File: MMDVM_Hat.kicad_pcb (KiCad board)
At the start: 2 copper layers, 65 x 56 mm, 107 parts, among them J1 Radio, J2 Raspberry_Pi_2_3, J7 GS2, J8 GS3, Q1 IRLML2060, Q2 2N7002, U1 LD1117S33TR, U2 STM32F722RETx, U3 MCP6002, U4 MCP6002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

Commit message: Revision 0.1
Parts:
- removed LEDs: FP_LEDs, Pin_Headers:Pin_Header_Straight_2x05_Pitch2.54mm
- added D10: POCSAG, LEDs:LED_0603, F.Cu at (29.2, 107.6)
- added G***: LOGO, MMDVM_logo:MMDVM_logo, F.Cu at (50.2, 77.7)
- added G***: LOGO, w_logo:Logo_silk_CC-BY-NC-SA_10x3.6mm, B.Cu at (25.2, 115.9)
- added J4: Panel LEDs, Pin_Headers:Pin_Header_Straight_2x10_Pitch2.00mm, F.Cu at (23.2, 107.6)
- added R33: 1k5, Resistors_SMD:R_0603, F.Cu at (32.8, 107.6)
- J7: footprint Connectors:GS2 -> jumper:SolderJumper-2_P1.3mm_Open_TrianglePad1.0x1.5mm
- J8: footprint Connectors:GS3 -> jumper:SolderJumper-3_P2.0mm_Open_TrianglePad1.0x1.5mm
- moved R6 8.31 mm to (32.8, 105.6)
- moved D5 8.30 mm to (29.2, 105.6)
- moved Radio TX 7.75 mm to (26.7, 116.3), turned to 90 degrees
- moved R11 6.11 mm to (32.8, 97.6)
- moved D9 6.10 mm to (29.2, 97.6)
- moved R7 4.71 mm to (32.8, 103.6)
- moved D6 4.70 mm to (29.2, 103.6)
- moved TX 4.35 mm to (31.1, 117.8), turned to 180 degrees
- moved STlink 3.72 mm to (21.5, 112.4)
- moved C22 3.23 mm to (39.0, 100.3)
- moved C23 3.23 mm to (39.0, 98.8)
- moved C11 3.16 mm to (37.5, 108.2), turned to 270 degrees
- moved C12 3.05 mm to (35.8, 108.2), turned to 270 degrees
- moved R9 2.52 mm to (32.8, 99.6)
- moved D8 2.50 mm to (29.2, 99.6)
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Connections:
- U2 pad 26: NXDN_LED -> Net-(U2-Pad26)
- U2 pad 33: Net-(U2-Pad33) -> SVC_LED
- U2 pad 34: PTT -> COS_LED
- U2 pad 35: COS_LED -> PTT
- U2 pad 36: SVC_LED -> DSTAR_LED
- U2 pad 37: Net-(U2-Pad37) -> DMR_LED
- U2 pad 38: DSTAR_LED -> YSF_LED
- U2 pad 39: DMR_LED -> P25_LED
- U2 pad 40: P25_LED -> NXDN_LED
- U2 pad 41: YSF_LED -> POCSAG_LED
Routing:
- net SVC_LED: track 48.3 -> 9.33 mm, vias 1 -> 0
- net COS_LED: track 40.0 -> 9.93 mm, vias 3 -> 0
- net DSTAR_LED: track 31.5 -> 12.0 mm, vias 2 -> 0
- net POCSAG_LED: track 0.00 -> 19.1 mm
- net YSF_LED: track 33.5 -> 14.9 mm, vias 2 -> 0
- net NXDN_LED: track 35.8 -> 17.7 mm, vias 3 -> 0
- net DMR_LED: track 31.0 -> 13.4 mm, vias 2 -> 0
- net +3V3: track 189.3 -> 206.1 mm
- net P25_LED: track 30.2 -> 16.3 mm
- net DAC_TX: track 32.4 -> 44.5 mm, vias 1 -> 2
- net Net-(D10-Pad2): track 0.00 -> 9.95 mm, vias 0 -> 1
- net Net-(D9-Pad2): track 1.75 -> 9.95 mm, vias 0 -> 1
- net Net-(D8-Pad2): track 1.75 -> 9.95 mm, vias 0 -> 1
- net Net-(D7-Pad2): track 1.75 -> 9.95 mm, vias 0 -> 1
- net Net-(D6-Pad2): track 1.75 -> 9.95 mm, vias 0 -> 1
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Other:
- outline, holes or cut-outs redrawn
- board text added: "12.000 MHz"
- board text added: "12.288 MHz"
- board text added: "14.400 MHz"
- board text added: "19.200 MHz"
- board text added: "Direct"
- board text added: "POCSAG"
- board text added: "Panel LEDs"
- board text added: "Revision 0.1"
- board text added: "Serial No:"
- board text added: "TCXO Frequency"
- board text added: "Trimmed"
- board text removed: "D*"

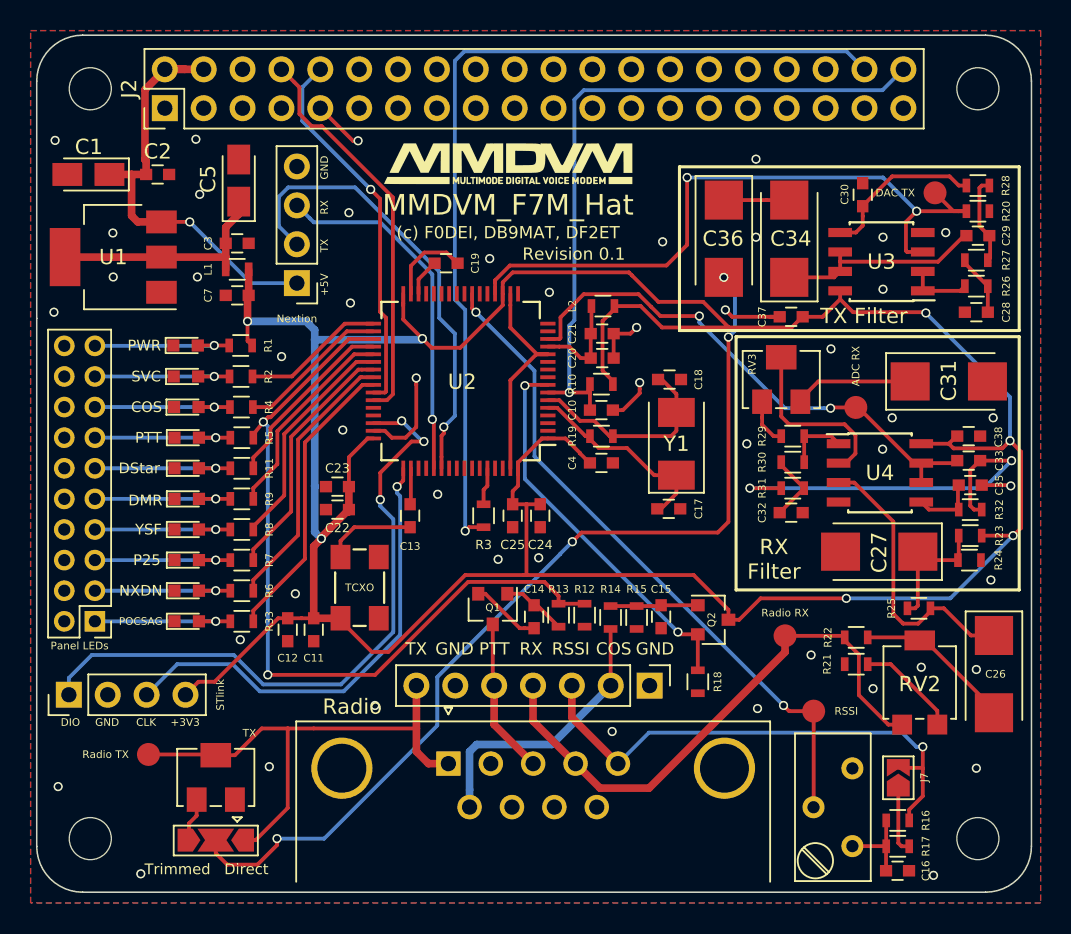
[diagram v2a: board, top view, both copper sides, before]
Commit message: Revision 0.2: Added FET for channel switching; Rename to MMDVM_RPT_Hat
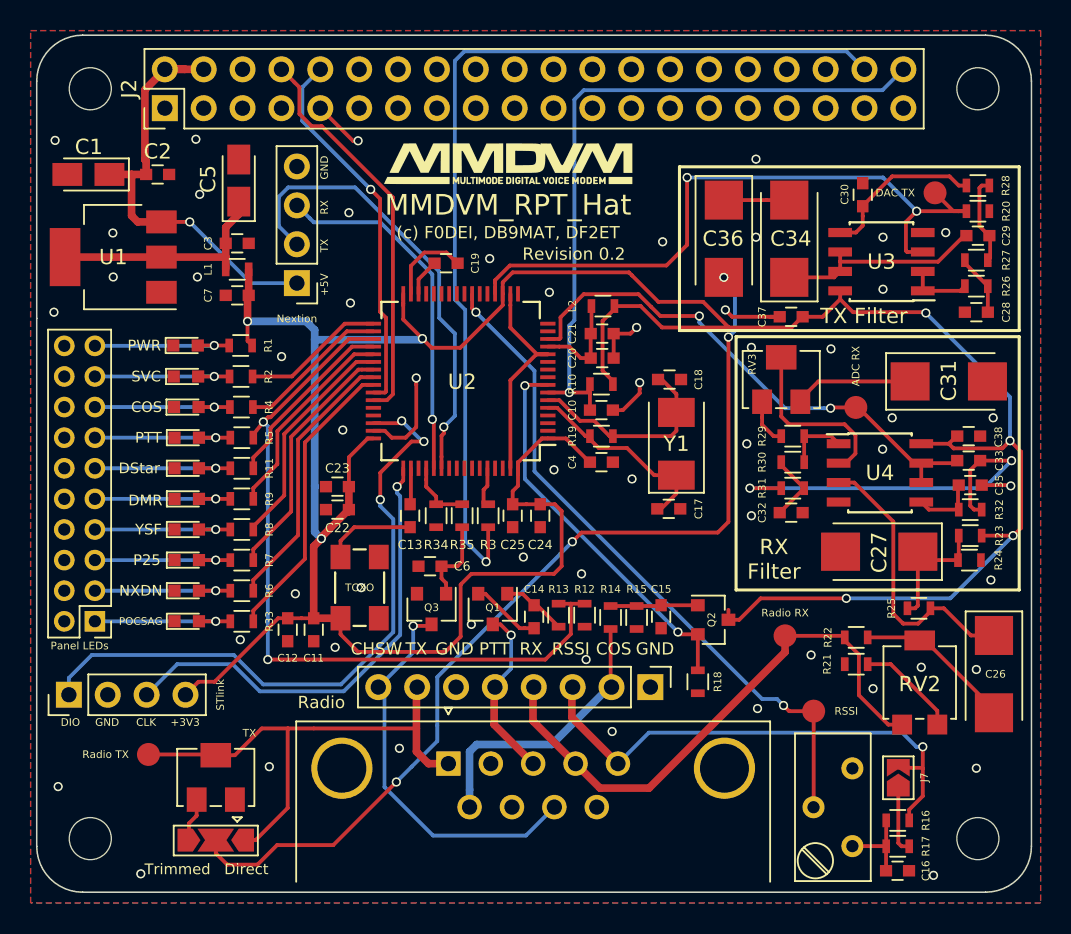
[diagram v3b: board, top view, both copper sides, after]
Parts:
- removed Radio: Radio, Pin_Headers:Pin_Header_Straight_1x07_Pitch2.54mm
- added C6: 470p, Capacitors_SMD:C_0603, F.Cu at (45.1, 104.0)
- added J5: Radio, Pin_Headers:Pin_Header_Straight_1x08_Pitch2.54mm, F.Cu at (59.5, 111.9)
- added Q3: IRLML2060, TO_SOT_Packages_SMD:SOT-23, F.Cu at (45.2, 106.8)
- added R34: 47k, Resistors_SMD:R_0603, F.Cu at (45.5, 100.7)
- added R35: 330, Resistors_SMD:R_0603, F.Cu at (47.2, 100.7)
- R19: value R -> 1M
- moved R3 0.30 mm to (48.9, 100.7)
- turned C4 to 180 degrees
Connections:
- C4 pad 1: +3V3 -> GND
- C4 pad 2: GND -> +3V3
- J1 pad 8: Net-(J1-Pad8) -> RADIO_CH_SW
- U2 pad 52: Net-(U2-Pad52) -> CH_SW
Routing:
- net RADIO_CH_SW: track 0.00 -> 26.1 mm, vias 0 -> 1
- net +3V3: track 206.1 -> 197.7 mm
- net Net-(C6-Pad1): track 0.00 -> 5.65 mm
- net CH_SW: track 0.00 -> 4.32 mm
- net Net-(J2-Pad38): track 59.8 -> 63.4 mm
- net RADIO_PTT: track 10.2 -> 11.5 mm, vias 0 -> 1
- net PTT: track 51.4 -> 50.5 mm
- net RSSI: track 43.7 -> 44.3 mm
- net GND: vias 48 -> 55
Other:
- board text added: "CHSW"
- board text added: "MMDVM_RPT_Hat"
- board text added: "Radio"
- board text added: "Revision 0.2"
- board text removed: "MMDVM_F7M_Hat"
- board text removed: "Revision 0.1"

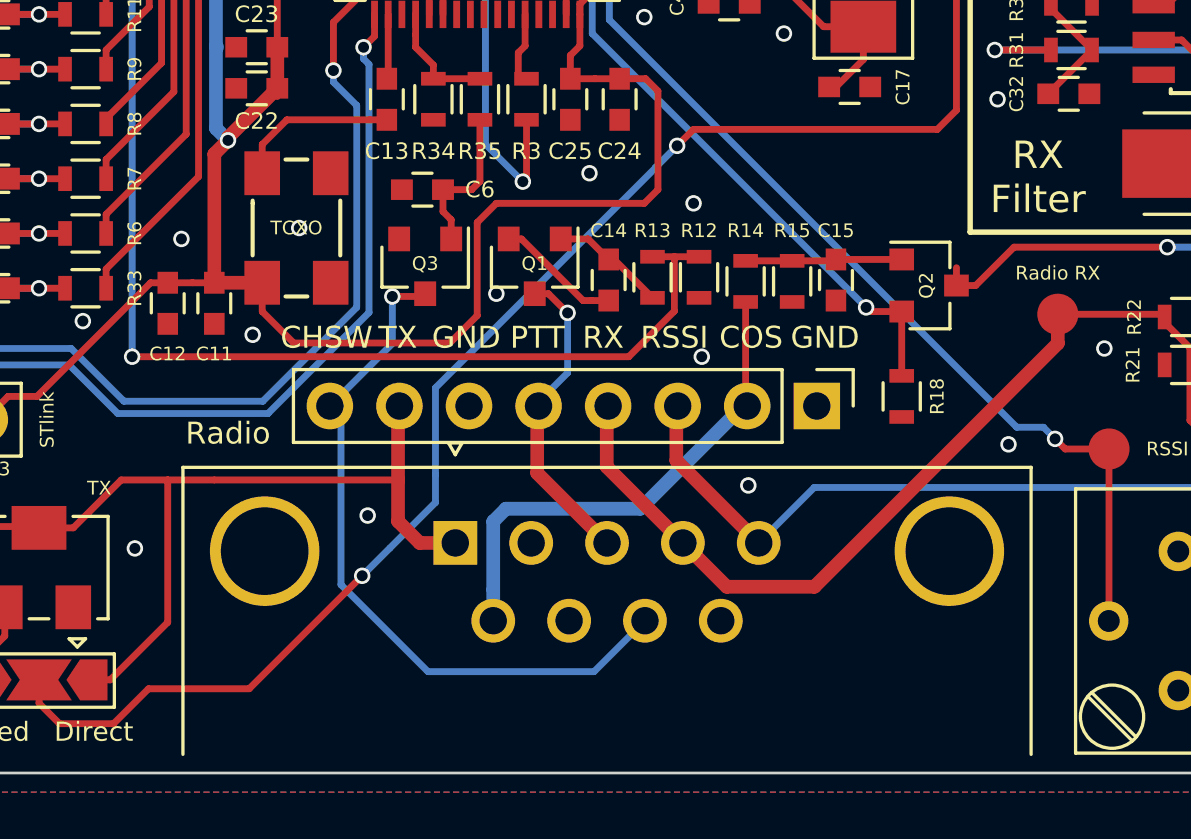
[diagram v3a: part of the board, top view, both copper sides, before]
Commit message: Aligned radio connector
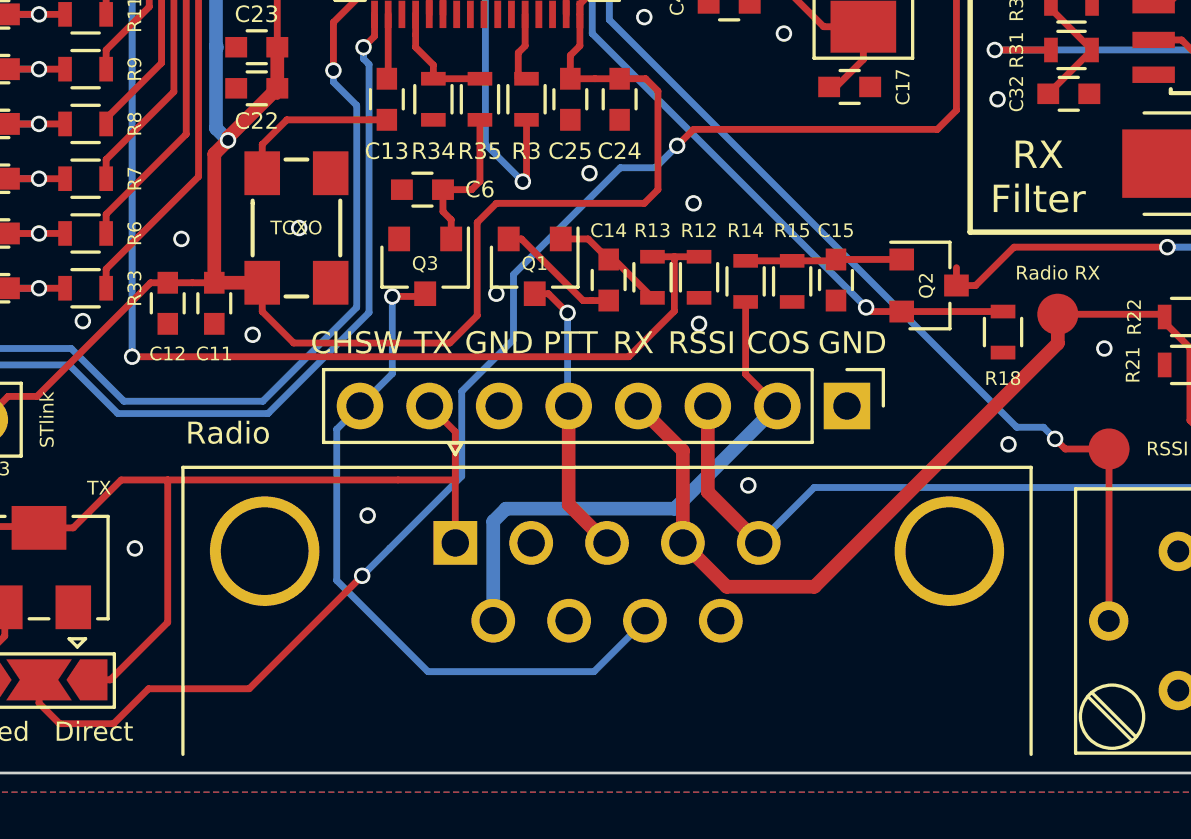
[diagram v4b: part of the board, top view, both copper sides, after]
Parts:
- moved R18 4.38 mm to (66.3, 109.2)
- moved J5 1.10 mm to (60.6, 111.9)
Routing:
- net RADIO_COS: track 18.3 -> 20.0 mm
- net COS: track 25.5 -> 26.8 mm
- net RADIO_PTT: track 11.5 -> 10.5 mm
- net Net-(C36-Pad2): track 62.9 -> 63.6 mm
- net RADIO_TX: track 34.0 -> 34.8 mm
- net R_RSSI: track 34.3 -> 33.7 mm
- net RADIO_RX: track 37.7 -> 37.1 mm

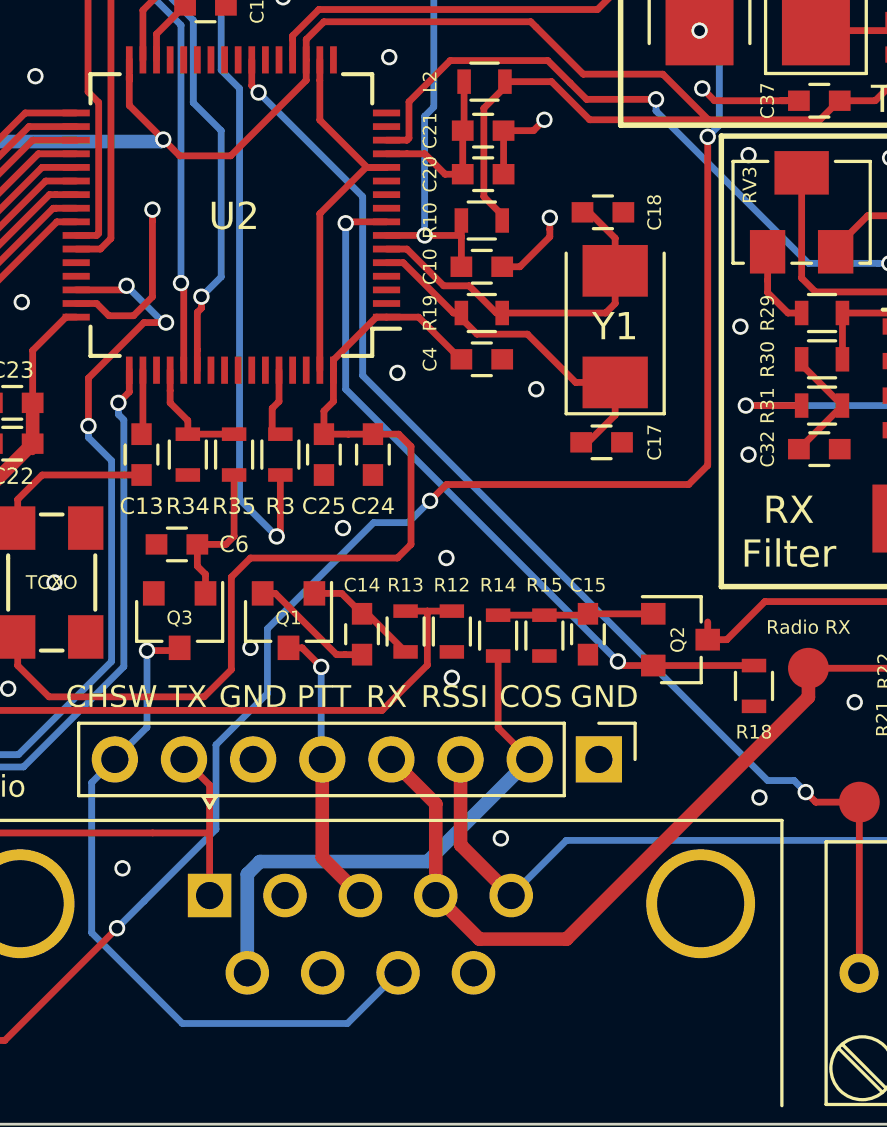
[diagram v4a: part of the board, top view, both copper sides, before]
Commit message: Added more GND vias
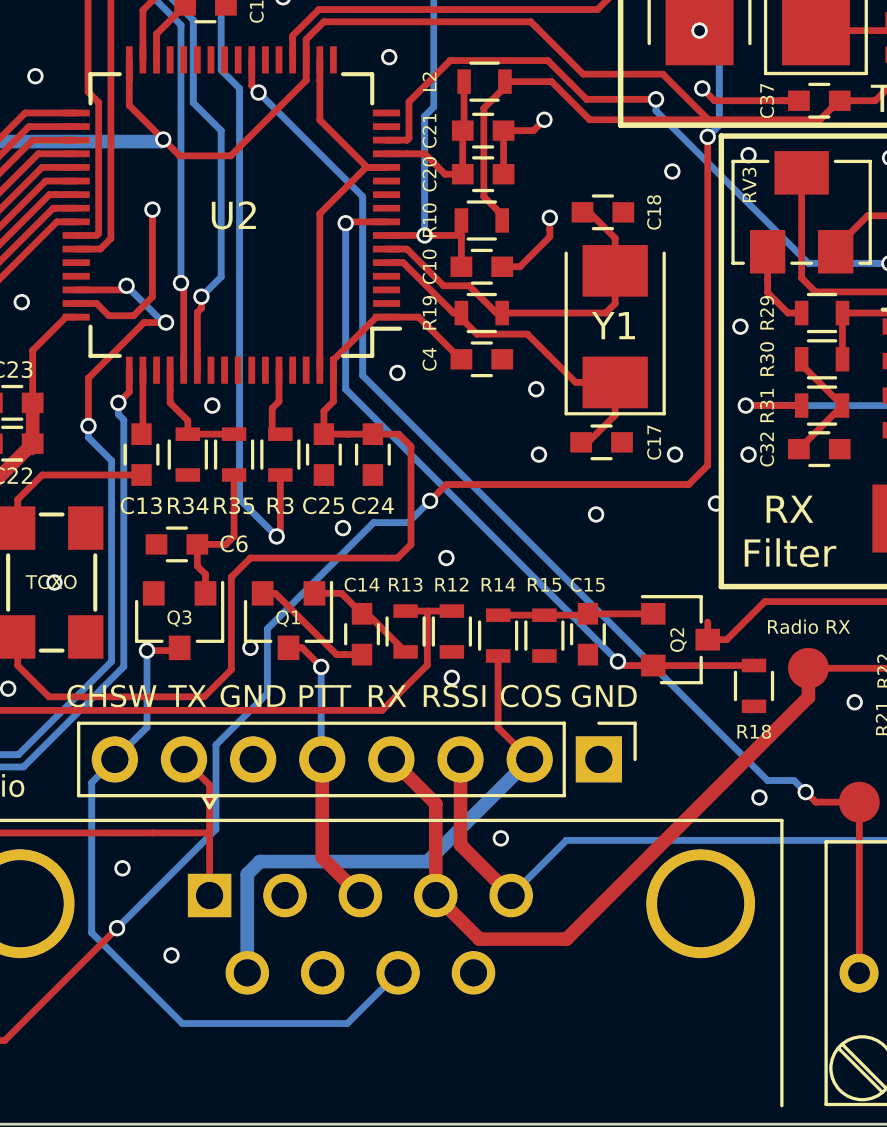
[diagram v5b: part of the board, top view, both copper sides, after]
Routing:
- net GND: vias 55 -> 62
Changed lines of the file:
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@@
     (thickness 1.6)
     (drawings 72)
-    (tracks 739)
+    (tracks 746)
     (zones 0)
     (modules 115)
@@
   (gr_line (start 22.4 125.3) (end 81.4 125.3) (angle 90) (layer Edge.Cuts) (width 0.1))
   (gr_line (start 84.4 72.3) (end 84.4 122.3) (angle 90) (layer Edge.Cuts) (width 0.1))
+  (via (at 46.4 98.9) (size 0.6) (drill 0.4) (layers F.Cu B.Cu) (net 28))
+  (via (at 63.3 90.3) (size 0.6) (drill 0.4) (layers F.Cu B.Cu) (net 28))
+  (via (at 63.4 100.7) (size 0.6) (drill 0.4) (layers F.Cu B.Cu) (net 28))
+  (via (at 64.9 102.5) (size 0.6) (drill 0.4) (layers F.Cu B.Cu) (net 28))
+  (via (at 60.5 102.9) (size 0.6) (drill 0.4) (layers F.Cu B.Cu) (net 28))
+  (via (at 58.4 100.7) (size 0.6) (drill 0.4) (layers F.Cu B.Cu) (net 28))
+  (via (at 44.9 119.1) (size 0.6) (drill 0.4) (layers F.Cu B.Cu) (net 28))
   (via (at 53.2 97.7) (size 0.6) (drill 0.4) (layers F.Cu B.Cu) (net 28))
   (via (at 38.9 109.3) (size 0.6) (drill 0.4) (layers F.Cu B.Cu) (net 28))
